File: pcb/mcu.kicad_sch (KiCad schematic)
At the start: 23 parts, among them J1 LCD, SW1 RESET, SW2 BOOT, U1 ESP32-S3-WROOM-1-N8R2

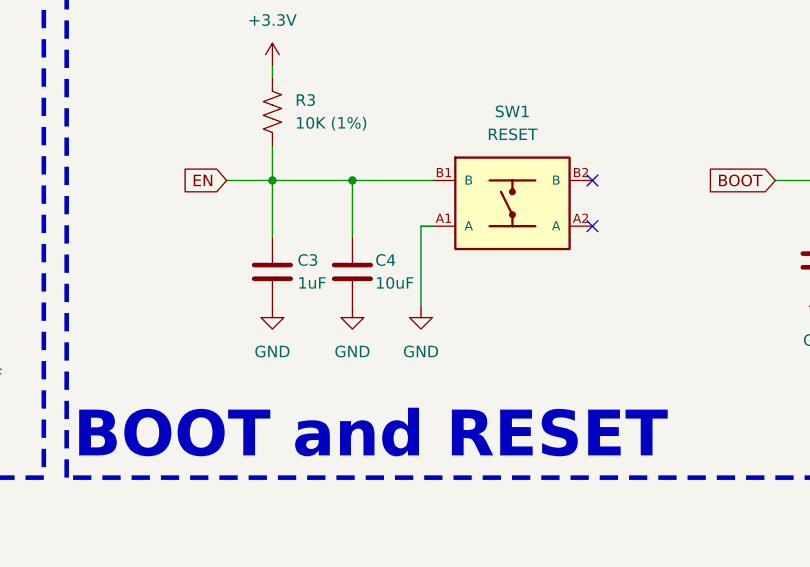
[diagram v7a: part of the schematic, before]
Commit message: Fixed cap values on reset button
Fixed all part numbers and extended parameters.
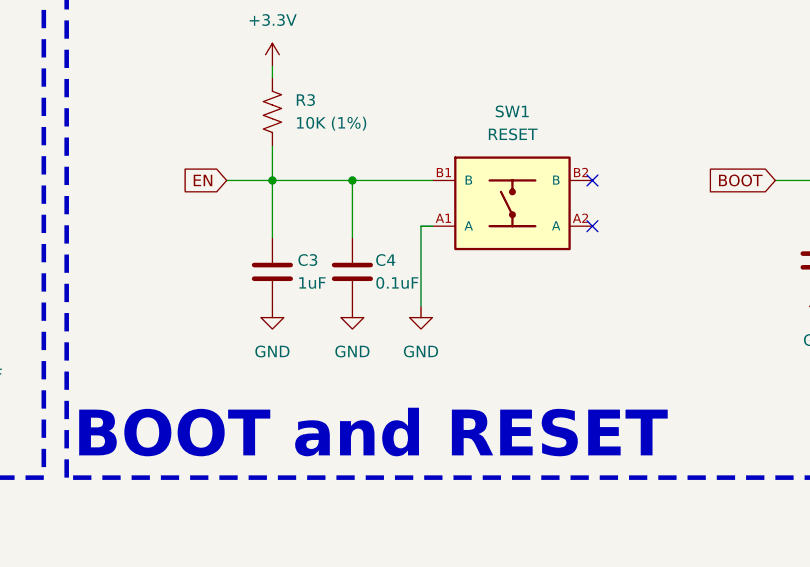
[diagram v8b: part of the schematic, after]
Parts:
- C1: Digikey (none) -> 1276-1005-2-ND; MF Samsung -> (none); Mouser (none) -> 187-CL10B104KO8NNNC
- C2: Digikey (none) -> 1276-1870-2-ND; LCSC_PN C92487 -> (none); MF Samsung -> (none); Mouser (none) -> 187-CL10A106MO8NQNC
- C3: Dielectric (none) -> X5R; Digikey (none) -> 1276-1019-2-ND; LCSC_PN C6119849 -> (none); MF HRE -> (none); Mouser (none) -> 187-CL10B105KO8NNNC; Tolerance (none) -> 10%; WVDC (none) -> 16V
- C4: value 10uF -> 0.1uF; Digikey (none) -> 1276-1005-2-ND; LCSC C92487 -> C66501; LCSC_PN C92487 -> (none); MF Samsung -> (none); MPN CL10A106MO8NQNC -> CL10B104KO8NNNC; Mouser (none) -> 187-CL10B104KO8NNNC
- C5: Digikey (none) -> 1276-1005-2-ND; LCSC_PN C66501 -> (none); MF Samsung -> (none); Mouser (none) -> 187-CL10B104KO8NNNC
- D1: LCSC_PN C2976072 -> (none); MF HRE -> (none); MN HRE -> World Semi
- J1: LCSC_PN C397114 -> (none); MF Omron -> (none)
- R1, R2: Digikey (none) -> CR0603-JW-103ELFTR-ND; LCSC_PN C2930027 -> (none); MF FOJAN -> (none); Mouser (none) -> 652-CR0603-JW-103ELF
- R3: Digikey (none) -> CR0603-FX-1002ELFTR-ND; LCSC_PN C103199 -> (none); MF Ralec -> (none); Mouser (none) -> 652-CR0603FX-1002ELF
- SW1, SW2: Digikey (none) -> P12931STR-ND; LCSC_PN C2976606 -> (none); MF Panasonic -> (none); Mouser (none) -> 667-EVQ-Q2B02W
- U1: Digikey (none) -> 5407-ESP32-S3-WROOM-1-N8R2-ND; LCSC_PN C2913204 -> (none); MF Espressif Systems -> (none); Mouser (none) -> 356-ESP32-S3WRM1N8R2
